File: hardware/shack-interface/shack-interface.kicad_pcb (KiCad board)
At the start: 4 copper layers, 160 x 161 mm, 295 parts, among them J1 RJ45 LINK, J10 R3 LED, J11 R1 mini-DIN, J12 R2 mini-DIN, J13 R3 mini-DIN, J14 USB4105-GF-A, J2 KILL switch, J3 13.8 V IN, J6 Front panel, J7 KILL state, J8 R1 LED, J9 R2 LED, Q11 BCP53-16, Q12 BC857B, Q13 BSS138BK, Q21 BCP53-16, Q22 BC857B, Q23 BSS138BK, Q31 BCP53-16, Q32 BC857B, Q33 BSS138BK, Q34 BC847B, Q41 BCP53-16, Q42 BC857B, Q44 BC847B, U1 L7805CV, U10 74LVC1G14, U11 74LVC1G02, U2 LD1117S33CTR, U201 74LVC1G08, U202 74LVC1G08, U203 TLP4176G, U204 TLP176AM, U205 PC817X, U3 TPS3823A-33, U301 74LVC1G08, U302 74LVC1G08, U303 TLP4176G, U304 TLP176AM, U305 PC817X, U4 74LVC1G74, U401 74LVC1G08, U402 74LVC1G08, U403 TLP4176G, U404 TLP176AM, U405 PC817X, U5 PCA9539, U6 TPS3823A-33, U61 USBLC6-2SC6, U7 74LVC1G14, U8 74LVC1G08, U9 74LVC1G74

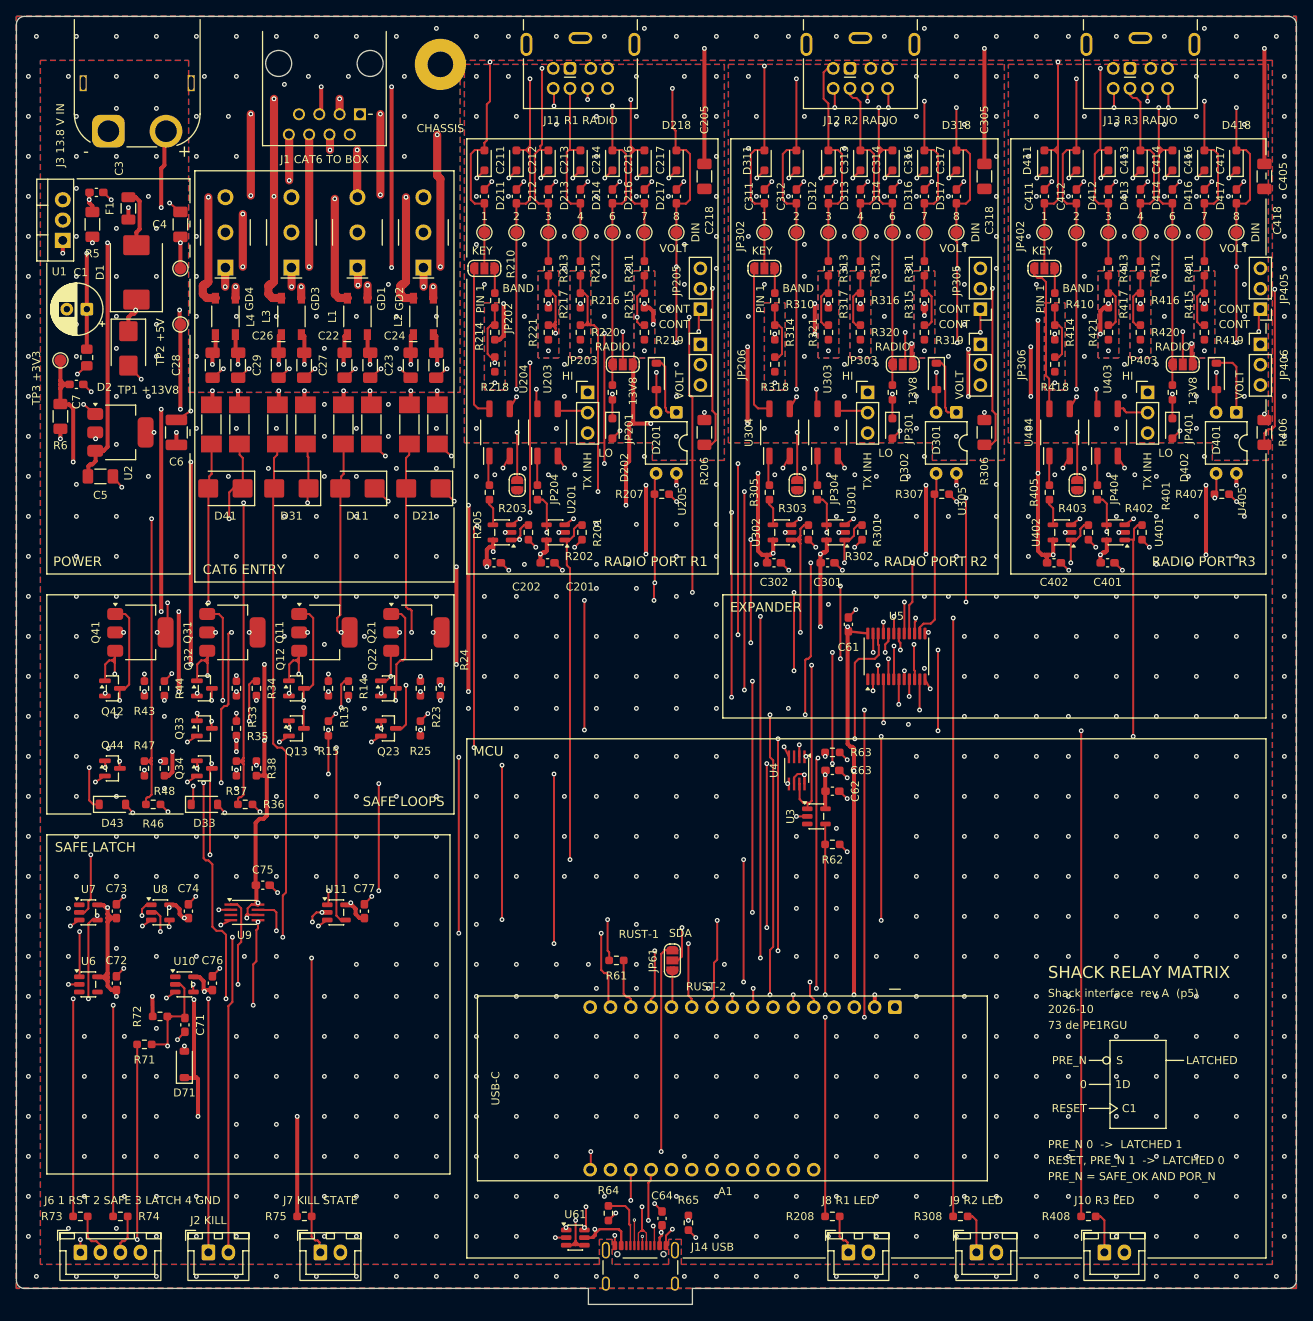
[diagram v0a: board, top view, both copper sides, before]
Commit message: Shack interface: end plates, schematic and PCB update; design log
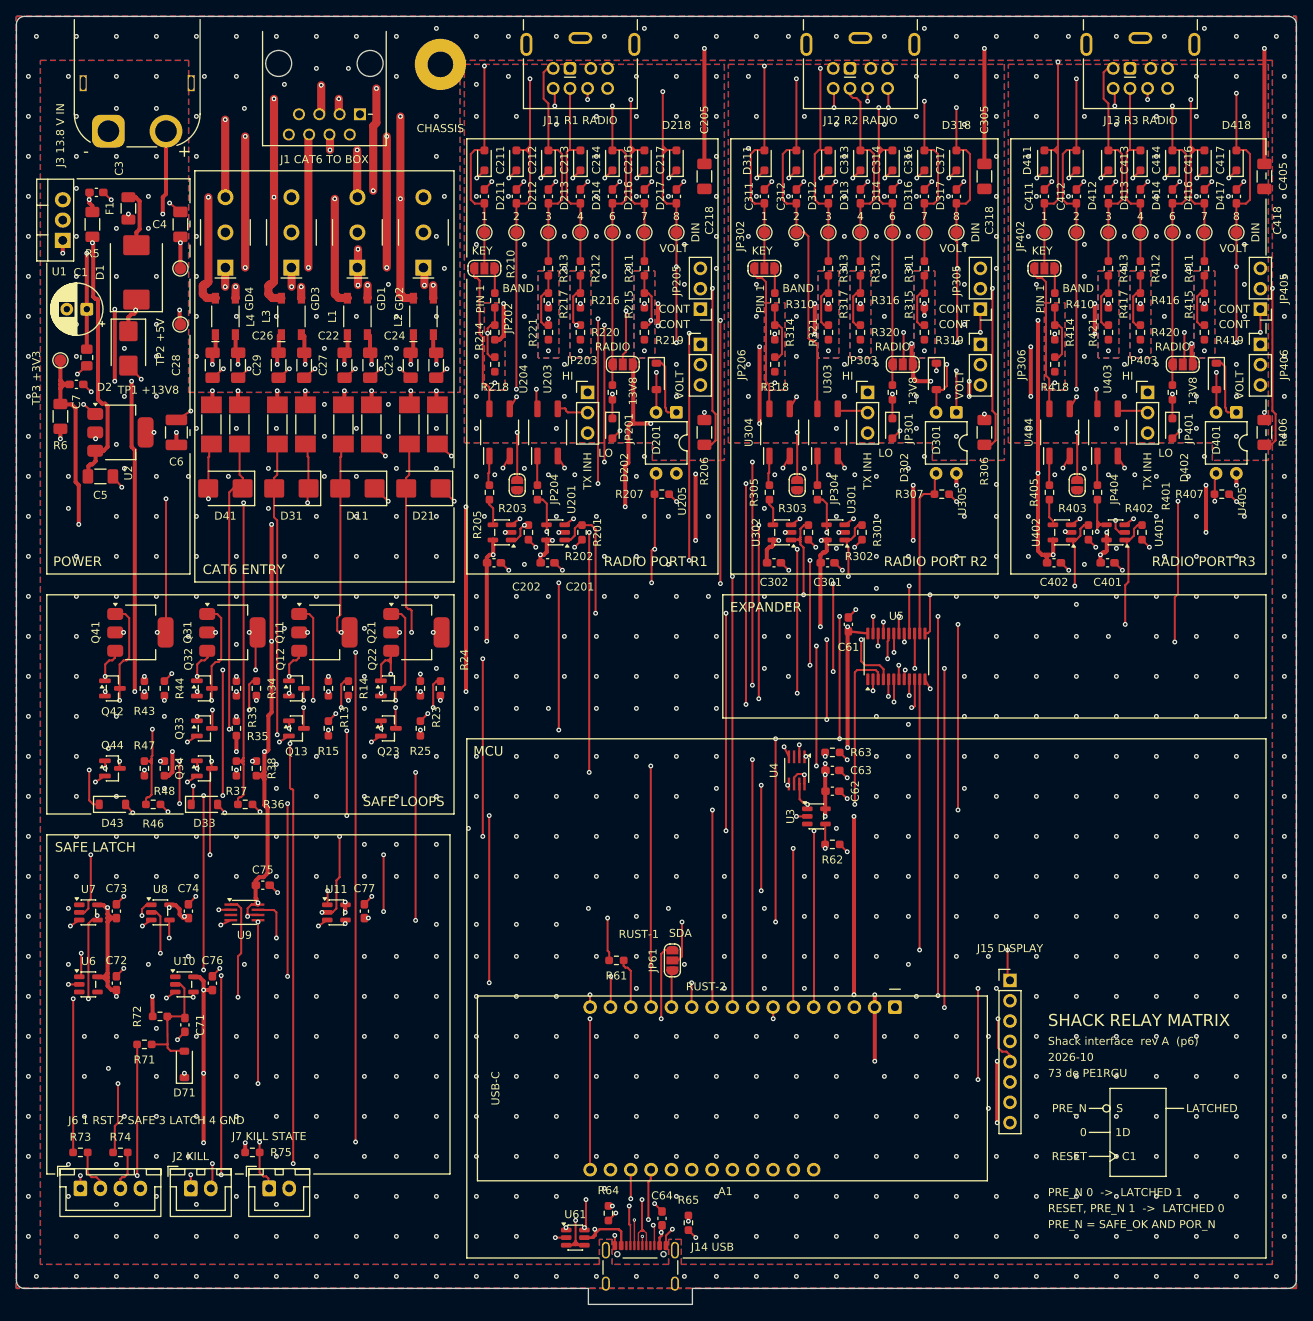
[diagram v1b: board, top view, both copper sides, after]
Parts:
- removed J10: R3 LED, Connector_JST:JST_XH_B2B-XH-A_1x02_P2.50mm_Vertical
- removed J8: R1 LED, Connector_JST:JST_XH_B2B-XH-A_1x02_P2.50mm_Vertical
- removed J9: R2 LED, Connector_JST:JST_XH_B2B-XH-A_1x02_P2.50mm_Vertical
- removed R208, R308, R408: 680R, Resistor_SMD:R_0603_1608Metric_Pad0.98x0.95mm_HandSolder
- added J15: DISPLAY, Connector_PinHeader_2.54mm:PinHeader_1x08_P2.54mm_Vertical, F.Cu at (144.2, 140.5)
- R75: value 10k -> 2k2
- moved R75 10.3 mm to (49.5, 162.0)
- moved J7 10.2 mm to (51.6, 166.5)
- moved J2 8.30 mm to (41.8, 166.5)
- moved J6 8.00 mm to (28.0, 166.5)
- moved R73 8.00 mm to (28.0, 162.0)
- moved R74 8.00 mm to (33.0, 162.0)
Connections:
- A1 pad 16: unconnected-(A1-IO9/BOOT-Pad16) -> /MCU and expander/DISP_MOSI
- A1 pad 7: unconnected-(A1-IO2-Pad7) -> /MCU and expander/DISP_SCK
- U5 pad 11: /MCU and expander/LED_R1 -> /MCU and expander/DISP_BL
- U5 pad 15: /MCU and expander/LED_R2 -> /MCU and expander/DISP_DC
- U5 pad 18: /MCU and expander/LED_R3 -> /MCU and expander/DISP_RST
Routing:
- net /MCU and expander/LED_R3: track 95.6 -> 0.00 mm, vias 4 -> 0
- net /MCU and expander/LED_R2: track 81.5 -> 0.00 mm, vias 2 -> 0
- net /MCU and expander/LED_R1: track 79.0 -> 0.00 mm, vias 4 -> 0
- net /MCU and expander/DISP_MOSI: track 0.00 -> 66.1 mm, vias 0 -> 3
- net /MCU and expander/DISP_RST: track 0.00 -> 63.7 mm, vias 0 -> 3
- net /MCU and expander/DISP_DC: track 0.00 -> 60.0 mm, vias 0 -> 3
- net /MCU and expander/DISP_BL: track 0.00 -> 48.9 mm, vias 0 -> 2
- net /MCU and expander/DISP_SCK: track 0.00 -> 36.0 mm, vias 0 -> 2
- net /MCU and expander/LATCHED: track 175.3 -> 160.9 mm
- net /Link to the box/R1_TX: track 109.4 -> 117.8 mm
- net /MCU and expander/BAND_C: track 97.7 -> 106.0 mm
- net /SAFE latch/SAFE_OK: track 48.3 -> 40.3 mm
- net /SAFE latch/BTN: track 33.1 -> 25.1 mm
- net /Link to the box/SW_STOP_N: track 93.9 -> 101.6 mm, vias 3 -> 5
- net /MCU and expander/KEY_R1: track 67.6 -> 74.4 mm
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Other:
- board text added: "J15 DISPLAY"
- board text added: "Shack interface rev A (p6)"
- board text removed: "J10 R3 LED"
- board text removed: "J8 R1 LED"
- board text removed: "J9 R2 LED"
- board text removed: "Shack interface rev A (p5)"
